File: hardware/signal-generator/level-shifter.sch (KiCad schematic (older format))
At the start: 27 parts

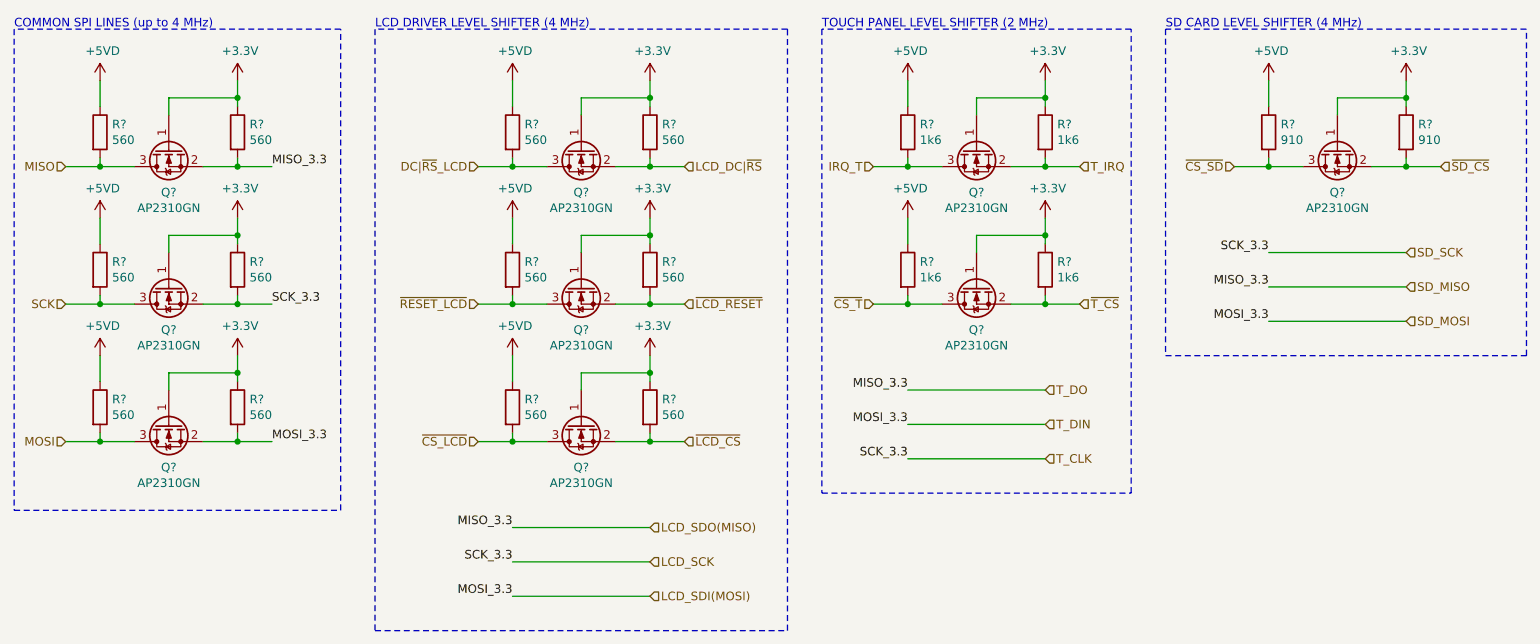
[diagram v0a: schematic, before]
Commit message: [Signal Generator] Add LCD module interface components
Since the LCD breakout board is to be connected to the project's PCB via
cable wires (i.e. the module won't be soldered directly to the PCB),
pin connectors have been added to the board. Additionally, the LCD
backlight is to be adjusted via the added MCP4551 digital potentiometer.
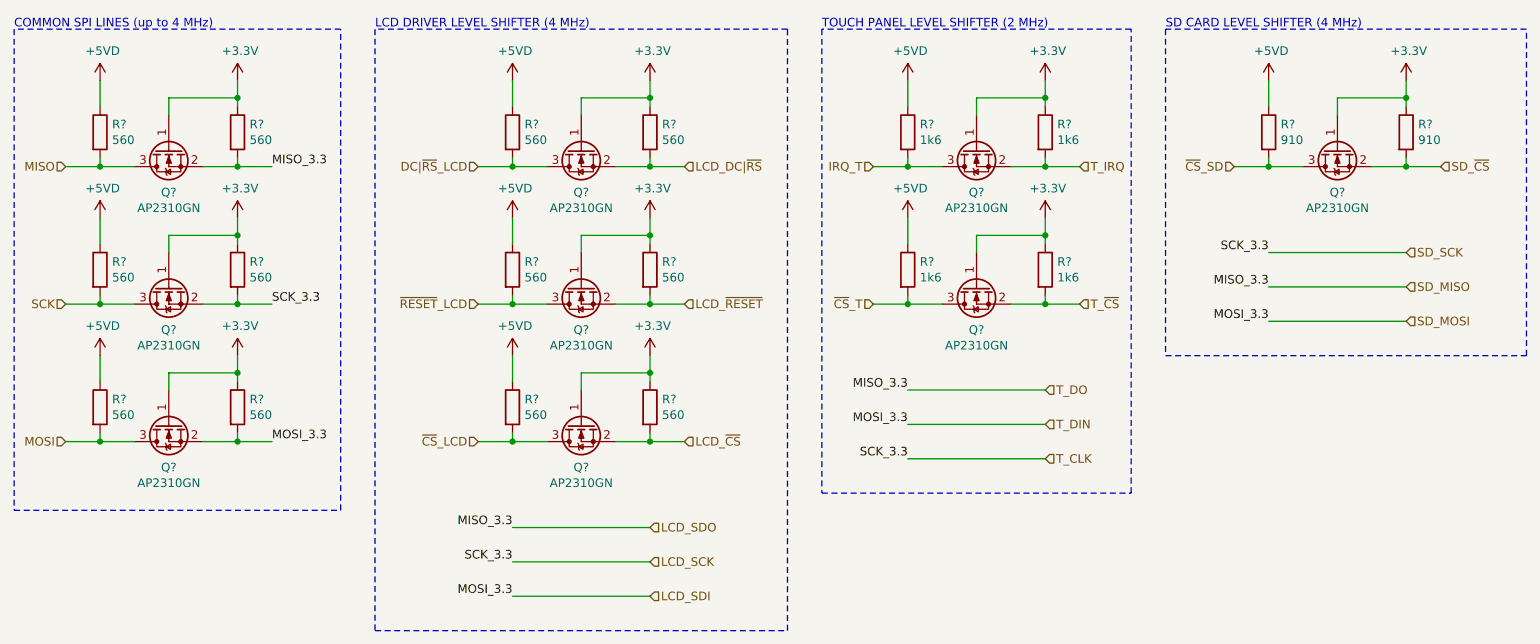
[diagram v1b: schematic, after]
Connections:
- net LCD_SDI(MOSI) renamed LCD_SDI
- net LCD_SDO(MISO) renamed LCD_SDO
- net ~CS_LCD renamed ~CS~_LCD
- net ~CS_SD renamed ~CS~_SD
- net ~CS_T renamed ~CS~_T
- net ~LCD_CS renamed LCD_~CS
- net ~LCD_RESET renamed LCD_~RESET
- net ~RESET_LCD renamed ~RESET~_LCD
- net ~SD_CS renamed SD_~CS
- net ~T_CS renamed T_~CS
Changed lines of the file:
@@
 $Descr A4 11693 8268
 encoding utf-8
-Sheet 5 5
+Sheet 5 6
 Title "Digital Function Generator v2 - Level Shifter"
 Date "2019-12-01"
@@
 $EndComp
 Text HLabel 10100 1950 2    50   Input ~ 0
-~SD_CS
+SD_~CS
 Text HLabel 8000 1950 2    50   Input ~ 0
 T_IRQ
@@
 T_DIN
 Text HLabel 8000 2750 2    50   Input ~ 0
-~T_CS
+T_~CS
 Text HLabel 7800 3650 2    50   Input ~ 0
 T_CLK
@@
 $EndComp
 Text HLabel 5500 4050 2    50   Input ~ 0
-LCD_SDO(MISO)
+LCD_SDO
 Text HLabel 5500 4450 2    50   Input ~ 0
-LCD_SDI(MOSI)
+LCD_SDI
 Text HLabel 5500 4250 2    50   Input ~ 0
 LCD_SCK
@@
 LCD_DC|~RS
 Text HLabel 5700 2750 2    50   Input ~ 0
-~LCD_RESET
+LCD_~RESET
 $Comp
 L ulib_MY_Transistor_FET:AP2310GN Q?
@@
 MISO
 Text HLabel 8900 1950 0    50   Input ~ 0
-~CS_SD
+~CS~_SD
 Text HLabel 6800 2750 0    50   Input ~ 0
-~CS_T
+~CS~_T
 Text HLabel 5700 3550 2    50   Input ~ 0
-~LCD_CS
+LCD_~CS
 $Comp
 L ulib_MY_Transistor_FET:AP2310GN Q?
@@
 $EndComp
 Text HLabel 4500 3550 0    50   Input ~ 0
-~CS_LCD
+~CS~_LCD
 Text HLabel 4500 2750 0    50   Input ~ 0
-~RESET_LCD
+~RESET~_LCD
 Text HLabel 4500 1950 0    50   Input ~ 0
 DC|~RS~_LCD

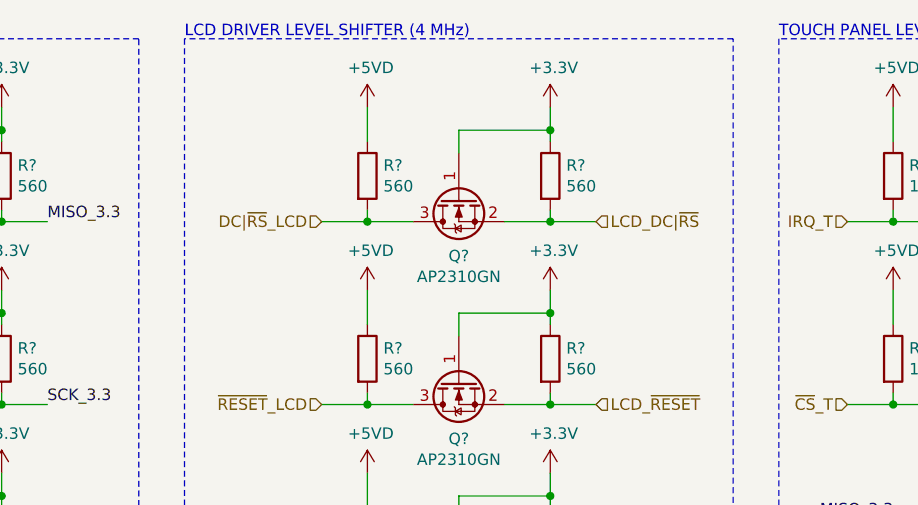
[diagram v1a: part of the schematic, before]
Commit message: [Signal Generator] Layout microcontroller and allocate its pins
The microcontroller is the brains of the function generator system - it
is responsible for controlling the DDS signal generator system, as well
as the LCD module which provides the user interface. The specific
microcontroller used in this project is the ATmega2561-16AU from the
megaAVR uC family. The reasons I have picked this particular part are
the following:
- I am familiar with the AVR uC structure;
- it provides more SRAM memory (8 kB) than other MCUs of the same family;
- it has fewer pins (and therefore peripherals) than the ATmega2560.
Only a fraction of the available peripheral pins of the ATmega2561 have
been utilized in the current design. The remaining port pins (which are
internally connected to useful peripherals such as JTAG, XMEM, etc.)
are connected to pin header connectors and are meant for
upgrading/modifying the system as a whole by including additional
external circuitry. The ATmega2561's SPI port is also connected to a
similar pin header connector which allows the uC to play the role of an
SPI slave device.
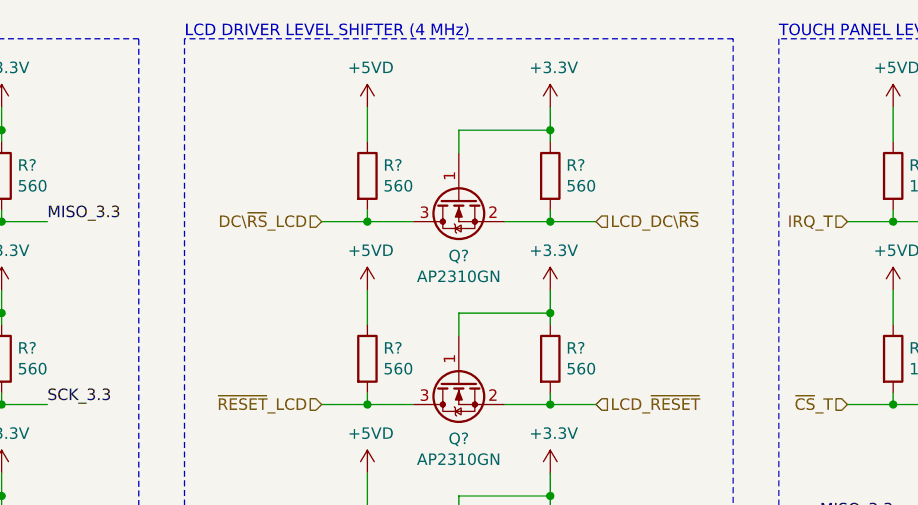
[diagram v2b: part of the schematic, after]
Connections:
- net DC|~RS~_LCD renamed DC\~RS~_LCD
- net LCD_DC|~RS renamed LCD_DC\~RS
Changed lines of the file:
@@
 $Descr A4 11693 8268
 encoding utf-8
-Sheet 5 6
+Sheet 6 6
 Title "Digital Function Generator v2 - Level Shifter"
 Date "2019-12-01"
@@
 LCD_SCK
 Text HLabel 5700 1950 2    50   Input ~ 0
-LCD_DC|~RS
+LCD_DC\~RS
 Text HLabel 5700 2750 2    50   Input ~ 0
 LCD_~RESET
@@
 ~RESET~_LCD
 Text HLabel 4500 1950 0    50   Input ~ 0
-DC|~RS~_LCD
+DC\~RS~_LCD
 Text HLabel 6800 1950 0    50   Input ~ 0
 IRQ_T
